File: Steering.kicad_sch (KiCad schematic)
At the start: 15 parts, among them U4 VOM618A-3T, U5 VOM618A-3T, U6 VOM618A-3T, U7 VOM618A-3T, U8 VOM618A-3T

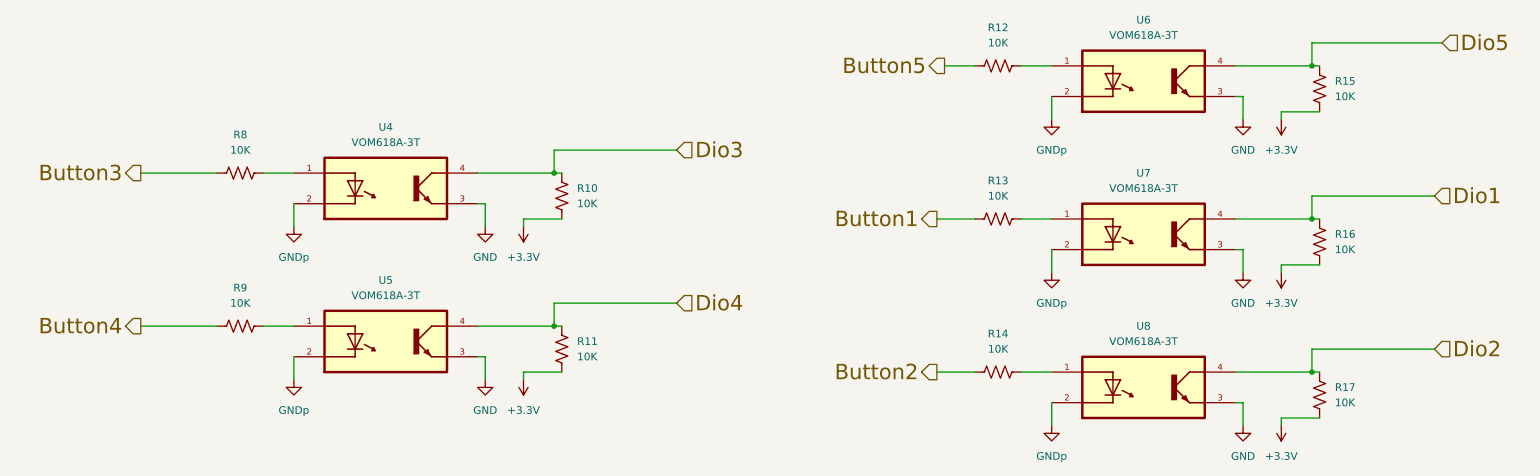
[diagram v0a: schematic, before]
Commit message: replaced CAN chip, power planes
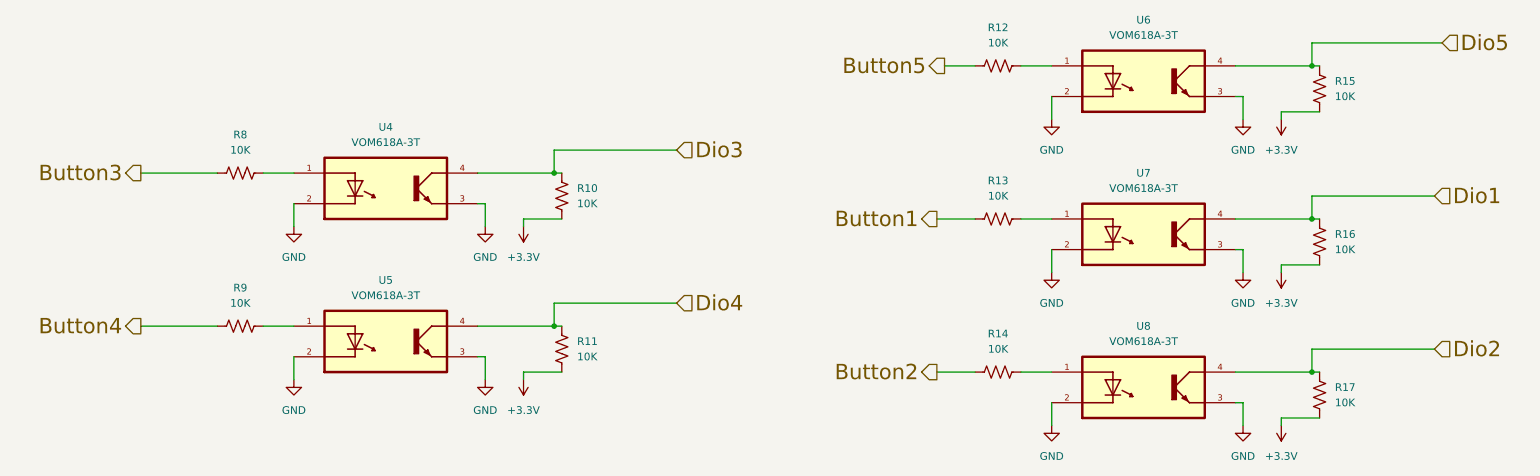
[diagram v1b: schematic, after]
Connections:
- net GNDp is gone; now on net GND: U4.2, U5.2, U6.2, U7.2, U8.2
